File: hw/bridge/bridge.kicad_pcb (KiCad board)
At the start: 2 copper layers, 54.6 x 42.9 mm, 56 parts, among them J1 USB_C_Receptacle_USB2.0_14P, J2 USB_C_Receptacle_USB2.0_14P, J3 DB9, J4 SWD, J5 BOOT, U1 STM32G0B1CBT, U2 MAX485E, U3 CH340E, U4 MCP1754S-3302xCB, U5 TJA1051T-3, U6 74LVC2G240, Y1 HCI XC53G2-8.000-F12NJHP

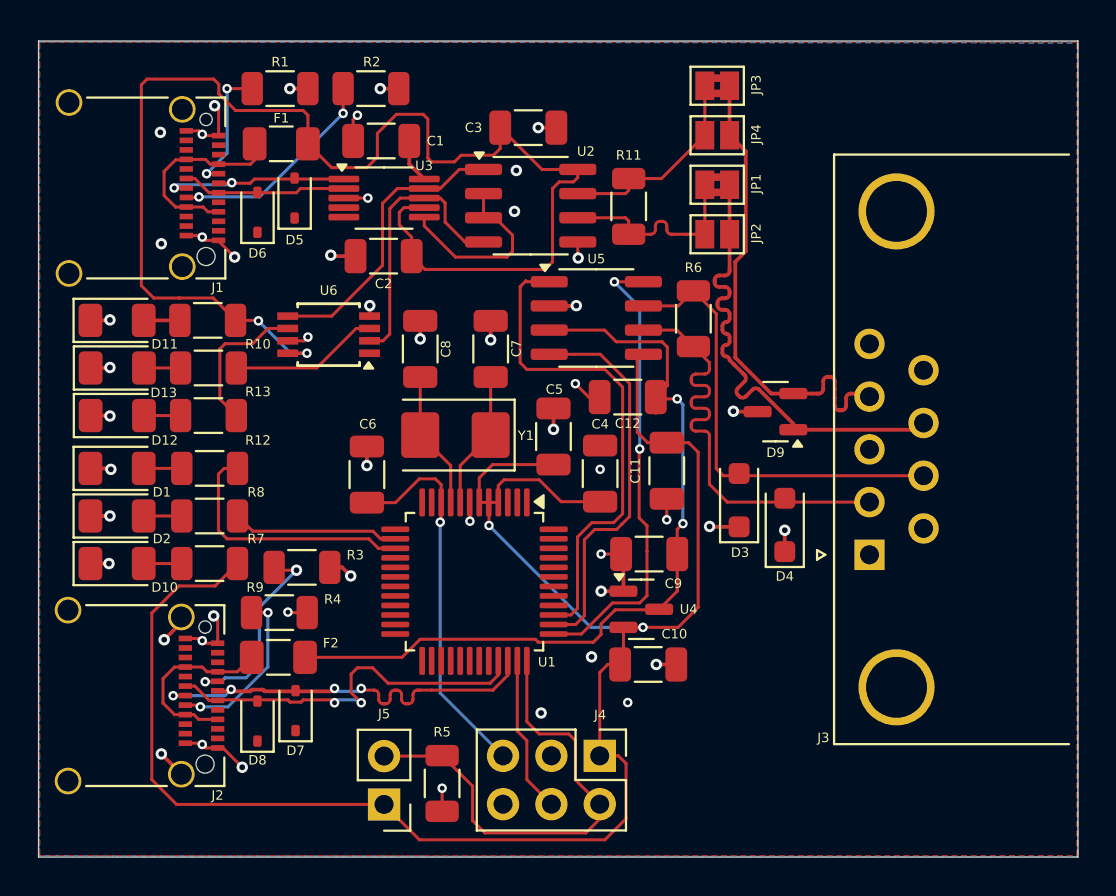
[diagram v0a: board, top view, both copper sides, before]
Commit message: Fix jumpers
Signed-off-by: Mateusz Pająk <22417805+Tai-Min@users.noreply.github.com>
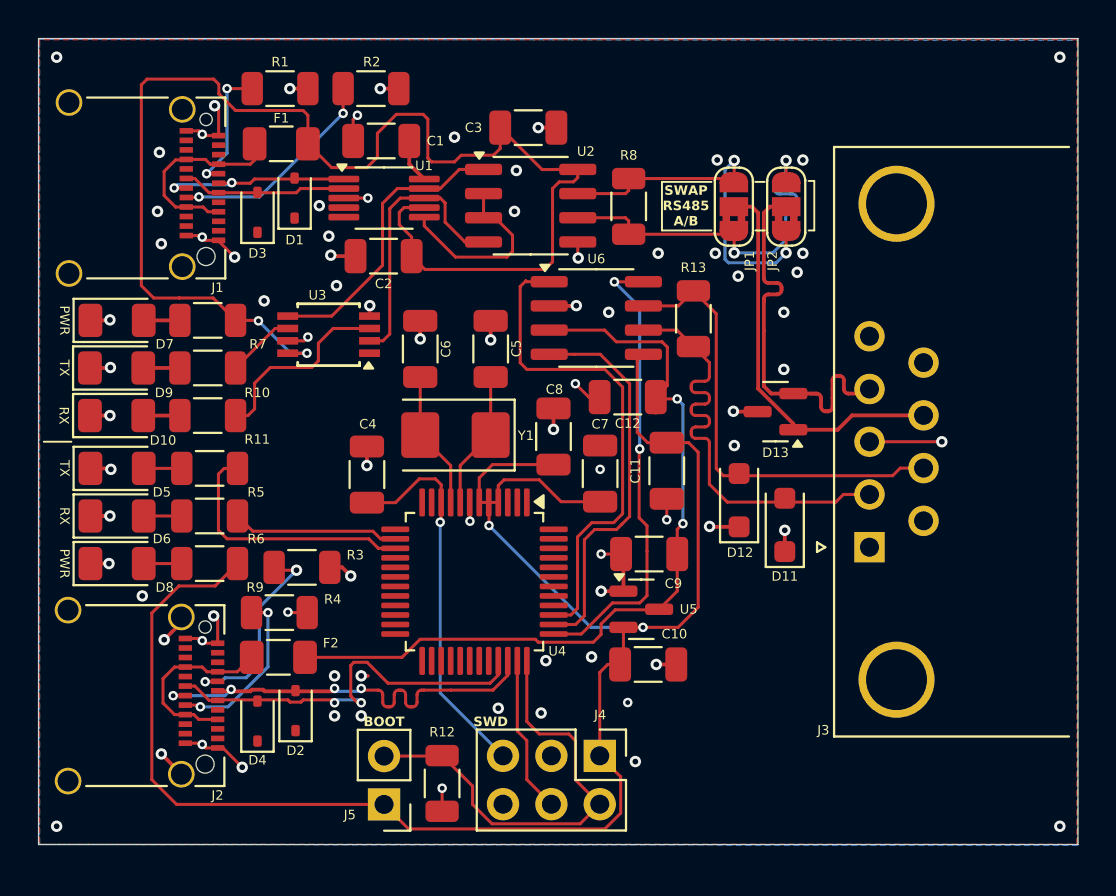
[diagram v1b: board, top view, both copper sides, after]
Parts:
- removed JP3: B, Jumper:SolderJumper-2_P1.3mm_Bridged2Bar_Pad1.0x1.5mm
- removed JP4: A, Jumper:SolderJumper-2_P1.3mm_Open_Pad1.0x1.5mm
- JP1: value A -> JMP; footprint Jumper:SolderJumper-2_P1.3mm_Bridged2Bar_Pad1.0x1.5mm -> Jumper:SolderJumper-3_P1.3mm_Bridged2Bar12_RoundedPad1.0x1.5mm
- JP2: value B -> JMP; footprint Jumper:SolderJumper-2_P1.3mm_Open_Pad1.0x1.5mm -> Jumper:SolderJumper-3_P1.3mm_Bridged2Bar12_RoundedPad1.0x1.5mm
- moved JP2 3.90 mm to (85.8, 112.8), turned to 90 degrees
- moved D10 2.50 mm to (50.6, 123.7)
- moved D9 2.50 mm to (50.6, 121.2)
- moved R10 2.50 mm to (55.4, 121.2)
- moved R11 2.50 mm to (55.4, 123.7)
- moved JP1 1.45 mm to (83.1, 112.8), turned to 90 degrees
- moved J3 0.40 mm to (90.2, 130.6)
- renumbered C6 to C4, C7 to C5, C8 to C6, C4 to C7, C5 to C8, D5 to D1, D13 to D10, D4 to D11, D3 to D12, D9 to D13, D7 to D2, D6 to D3, D8 to D4, D1 to D5, D2 to D6, D11 to D7, D10 to D8, D12 to D9, R12 to R10, R13 to R11, R5 to R12, R6 to R13, R8 to R5, R7 to R6, R10 to R7, R11 to R8, U3 to U1, U6 to U3, U1 to U4, U4 to U5, U5 to U6
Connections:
- JP2 pad 1: /MODBUS+ -> /MODBUS-
- JP2 pad 2: /M+ -> /M-
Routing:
- net /MODBUS-: track 10.9 -> 20.4 mm, vias 0 -> 2
- net /MODBUS+: track 10.9 -> 20.4 mm, vias 0 -> 2
- net /M+: track 25.5 -> 20.7 mm
- net /M-: track 25.6 -> 20.9 mm
- net Net-(R10-Pad2): track 7.87 -> 3.60 mm
- net GND: track 53.9 -> 58.2 mm, vias 50 -> 80
- net Net-(R11-Pad2): track 7.86 -> 10.3 mm
- net +3.3V: track 98.8 -> 97.2 mm
- net /mcu/USB+: track 22.4 -> 23.1 mm
- net /mcu/USB-: track 20.8 -> 21.4 mm
- net /mcu/SWCLK: track 25.2 -> 24.6 mm
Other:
- board size 54.6 x 42.9 mm -> 54.6 x 42.3 mm
- board text added: "BOOT"
- board text added: "PWR"
- board text added: "RX"
- board text added: "SWAP RS485 A/B"
- board text added: "SWD"
- board text added: "TX"

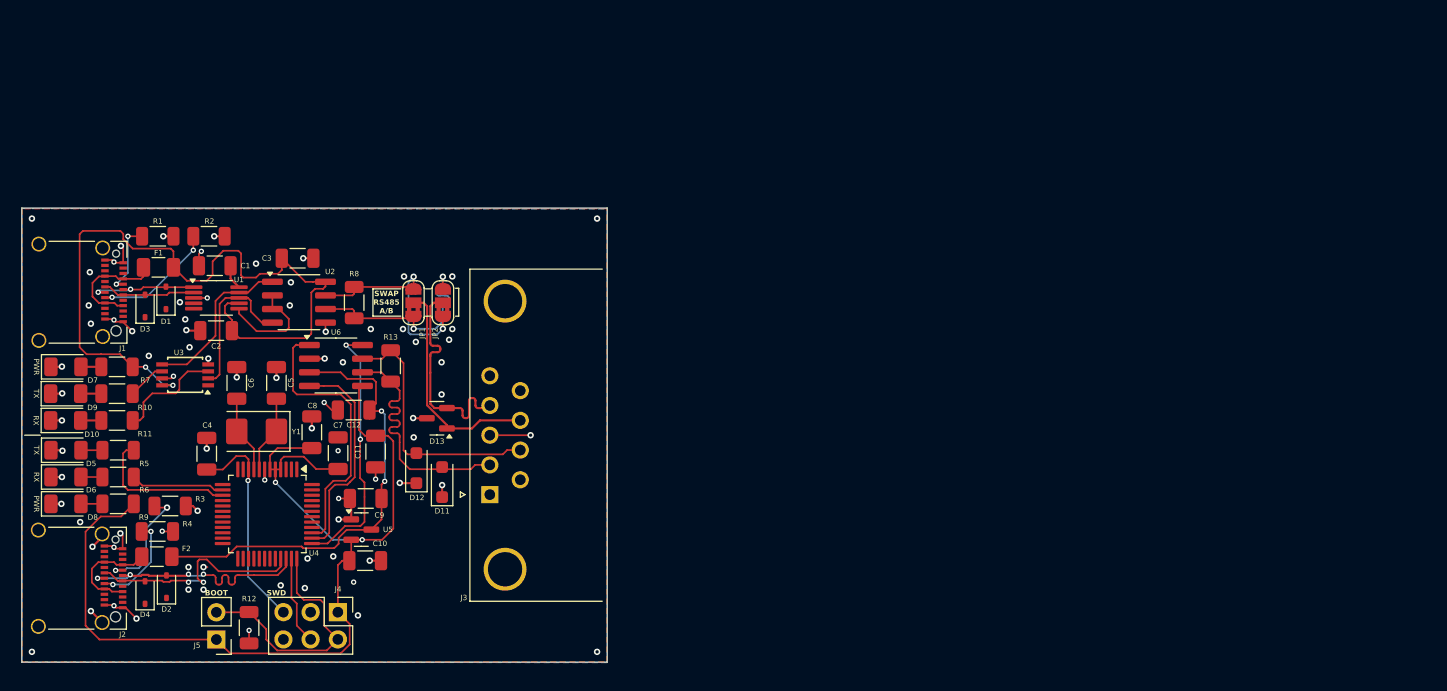
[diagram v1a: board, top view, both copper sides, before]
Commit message: Redesign the PCB, remove DNP components
Signed-off-by: Mateusz Pająk <22417805+Tai-Min@users.noreply.github.com>
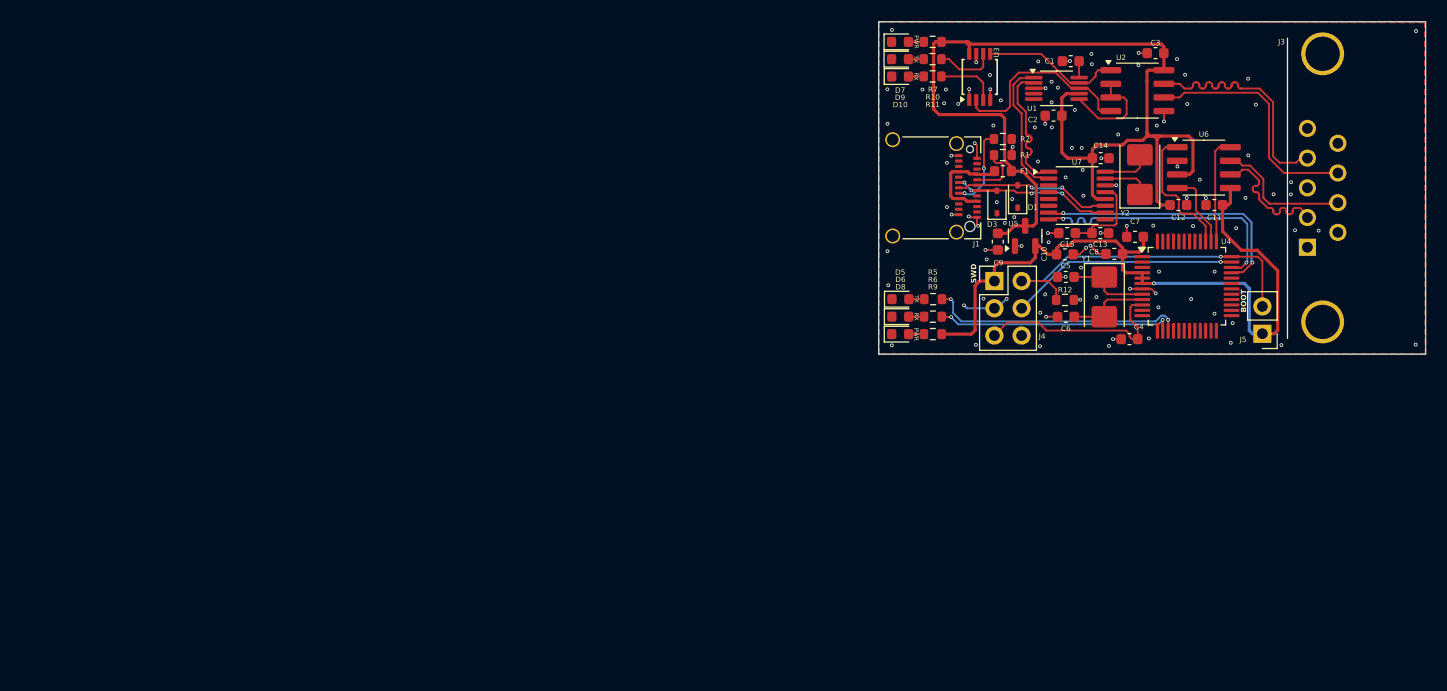
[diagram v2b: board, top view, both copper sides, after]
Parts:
- removed D11, D12: PTVS20VS1UR,115-ES, Diode_SMD:D_SOD-123F
- removed D13: SM712, Package_TO_SOT_SMD:SOT-23
- removed D2, D4: PTVSHC3D4V5B, Diode_SMD:D_SOD-323
- removed F2: 500mA, Fuse:Fuse_1206_3216Metric
- removed J2: USB_C_Receptacle_USB2.0_14P, Connector_USB:USB_C_Receptacle_Amphenol_12401610E4-2A_CircularHoles
- removed JP1, JP2: JMP, Jumper:SolderJumper-3_P1.3mm_Bridged2Bar12_RoundedPad1.0x1.5mm
- removed R13, R8: 120R, Resistor_SMD:R_1206_3216Metric
- removed R3, R4: 5.1k, Resistor_SMD:R_1206_3216Metric
- added C13: 100n / 16V, Capacitor_SMD:C_0603_1608Metric, F.Cu at (147.1, 106.3)
- added C14: 1u / 16V, Capacitor_SMD:C_0603_1608Metric, F.Cu at (147.2, 99.3)
- added C15: 10u / 16V, Capacitor_SMD:C_0603_1608Metric, F.Cu at (144.0, 106.3)
- added U7: CH334R, Package_SO:QSOP-16_3.9x4.9mm_P0.635mm, F.Cu at (144.9, 102.8)
- added Y2: HCI XC53G2-12.000-F20LJDT, Crystal:Crystal_SMD_5032-2Pin_5.0x3.2mm, F.Cu at (150.8, 100.8)
- C1, C10, C11, C12, C2, C3, C5, C7, C8, C9: footprint Capacitor_SMD:C_1206_3216Metric -> Capacitor_SMD:C_0603_1608Metric
- C4: value 100n / 50V -> 100n / 16V; footprint Capacitor_SMD:C_1206_3216Metric -> Capacitor_SMD:C_0603_1608Metric
- C6: value 6p / 50V -> 6p / 16V; footprint Capacitor_SMD:C_1206_3216Metric -> Capacitor_SMD:C_0603_1608Metric
- D10, D5, D6, D7, D8, D9: footprint LED_SMD:LED_1206_3216Metric -> LED_SMD:LED_0603_1608Metric
- F1: footprint Fuse:Fuse_1206_3216Metric -> Fuse:Fuse_0603_1608Metric
- R1, R10, R11, R12, R2, R5, R6, R7, R9: footprint Resistor_SMD:R_1206_3216Metric -> Resistor_SMD:R_0603_1608Metric
- moved J5 101.6 mm to (162.2, 115.6)
- moved U4 88.3 mm to (155.2, 111.2), turned to 0 degrees
- moved C4 86.7 mm to (149.8, 116.1), turned to 0 degrees
- moved D10 84.2 mm to (128.5, 91.7)
- moved D9 83.8 mm to (128.4, 90.0)
- moved D7 83.5 mm to (128.4, 88.4)
- moved U6 83.0 mm to (156.8, 100.2)
- moved R11 82.5 mm to (131.5, 91.6)
- moved C3 82.2 mm to (152.3, 89.5), turned to 0 degrees
- moved R10 82.2 mm to (131.5, 90.0)
- moved C1 82.1 mm to (144.4, 90.2)
- moved R12 82.0 mm to (143.8, 112.5), turned to 0 degrees
- moved R7 81.9 mm to (131.5, 88.4)
- moved C11 81.5 mm to (157.8, 103.6), turned to 0 degrees
- moved U1 80.7 mm to (143.0, 92.8)
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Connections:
- net /can/RX renamed /mcu/CAN_RX
- net /can/S renamed /mcu/CAN_S
- net /can/TX renamed /mcu/CAN_TX
- C12 pad 2: +5C -> +5V
- C9 pad 2: +5C -> +5V
- D1 pad 2: /RS_D+ -> /D+
- D3 pad 2: /RS_D- -> /D-
- J1 pad A6: /RS_D+ -> /D+
- J1 pad A7: /RS_D- -> /D-
- J1 pad B6: /RS_D+ -> /D+
- J1 pad B7: /RS_D- -> /D-
- U1 pad 1: /RS_D+ -> /D_RS+
- U1 pad 2: /RS_D- -> /D_RS-
- U2 pad 6: /MODBUS+ -> /M+
- U2 pad 7: /MODBUS- -> /M-
- U4 pad 33: /mcu/USB- -> /D_CAN-
- U4 pad 34: /mcu/USB+ -> /D_CAN+
- U5 pad 3: +5C -> +5V
- U6 pad 3: +5C -> +5V
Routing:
- net +5C: track 43.3 -> 0.00 mm, vias 2 -> 0
- net +3.3V: track 97.2 -> 67.6 mm, vias 2 -> 1
- net +5V: track 72.0 -> 101.3 mm, vias 2 -> 0
- net /D_CAN-: track 0.00 -> 25.5 mm, vias 0 -> 2
- net /D_CAN+: track 0.00 -> 25.4 mm, vias 0 -> 2
- net GND: track 58.2 -> 34.6 mm, vias 80 -> 109
- net /mcu/USB+: track 23.1 -> 0.00 mm, vias 4 -> 0
- net /mcu/USB-: track 21.4 -> 0.00 mm, vias 2 -> 0
- net /MODBUS-: track 20.4 -> 0.00 mm, vias 2 -> 0
- net /MODBUS+: track 20.4 -> 0.00 mm, vias 2 -> 0
- net /D-: track 0.00 -> 16.9 mm, vias 0 -> 4
- net /D+: track 0.00 -> 14.8 mm, vias 0 -> 2
- net /mcu/CAN_S: track 24.5 -> 10.0 mm, vias 2 -> 0
- net /mcu/LED_RX: track 8.78 -> 22.2 mm, vias 0 -> 2
- net /mcu/CAN_TX: track 26.3 -> 12.9 mm
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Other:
- board size 54.6 x 42.3 mm -> 51 x 31 mm
- board text removed: "SWAP RS485 A/B"

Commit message: Add datasheets, add BOM links
Signed-off-by: Mateusz Pająk <22417805+Tai-Min@users.noreply.github.com>
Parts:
- C1: value 100n -> 100n / 16V
- C6: value 6p / 16V -> 6p / 50V
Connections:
- net /M+ renamed /MODBUS+
- net /M- renamed /MODBUS-

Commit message: Minor fixes
Signed-off-by: Mateusz Pająk <22417805+Tai-Min@users.noreply.github.com>
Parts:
- removed the U3 at (135.9, 91.7)
- added C4: 1u, Capacitor_SMD:C_0603_1608Metric, F.Cu at (133.1, 108.6)
- added R12: 0, Resistor_SMD:R_0603_1608Metric, F.Cu at (162.1, 99.4)
- added R13: 0, Resistor_SMD:R_0603_1608Metric, F.Cu at (162.1, 100.9)
- added R14: 0, Resistor_SMD:R_0603_1608Metric, F.Cu at (155.9, 93.7)
- added R15: 0, Resistor_SMD:R_0603_1608Metric, F.Cu at (155.9, 92.2)
- added R3: 10k, Resistor_SMD:R_0603_1608Metric, F.Cu at (138.5, 89.4)
- added R4: 10k, Resistor_SMD:R_0603_1608Metric, F.Cu at (151.4, 104.7)
- added REF**: OSHW-Logo2_7.3x6mm_SilkScreen, Symbol:OSHW-Logo2_7.3x6mm_SilkScreen, F.Cu at (160.6, 92.5)
- added REF**: KiCad-Logo2_5mm_SilkScreen, Symbol:KiCad-Logo2_5mm_SilkScreen, B.Cu at (134.0, 90.2)
- added U4: 74LVC2G04, Package_TO_SOT_SMD:SOT-23-6, F.Cu at (135.4, 91.2)
- C1: renamed from C2; value 100n / 16V -> 100n
- C10: renamed from C11; value 100n / 16V -> 100n
- C11: renamed from C12; value 100n / 16V -> 100n
- C12: renamed from C4; value 100n / 16V -> 100n
- C13: renamed from C5; value 6p / 50V -> 6p
- C14: renamed from C6; value 6p / 50V -> 6p
- C15: renamed from C7; value 100n / 16V -> 100n
- C16: renamed from C8; value 100n / 16V -> 100n
- C2: renamed from C1; value 100n / 16V -> 100n
- C3: value 100n / 16V -> 100n
- C5: renamed from C15; value 10u / 16V -> 10u
- C6: renamed from C13; value 100n / 16V -> 100n
- C7: renamed from C14; value 1u / 16V -> 1u
- C8: renamed from C9; value 10u / 16V -> 10u
- C9: renamed from C10; value 10u / 16V -> 10u
- J2: renamed from J3; value DB9 -> DE9
- moved C3 27.9 mm to (133.5, 110.1), turned to 180 degrees
- moved D5 3.14 mm to (128.5, 91.6)
- moved R7 3.14 mm to (131.5, 91.6)
- moved D3 1.69 mm to (128.4, 88.3)
- moved D4 1.69 mm to (128.5, 90.0)
- moved R5 1.69 mm to (131.5, 88.3)
- moved R6 1.69 mm to (131.5, 90.0)
- renumbered D3 to D2, D9 to D3, D10 to D4, D7 to D5, D5 to D6, D6 to D7, J4 to J3, J5 to J4, R9 to R10, R12 to R11, R10 to R5, R11 to R6, R5 to R8, R6 to R9, U7 to U3, U4 to U7, Y2 to Y1, Y1 to Y2
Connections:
- C3 pad 2: +5V -> /VUSB
- F1 pad 1: Net-(F1-Pad1) -> /VUSB
- J1 pad A4: Net-(F1-Pad1) -> /VUSB
- J1 pad A9: Net-(F1-Pad1) -> /VUSB
- J1 pad B4: Net-(F1-Pad1) -> /VUSB
- J1 pad B9: Net-(F1-Pad1) -> /VUSB
- U2 pad 6: /MODBUS+ -> Net-(U2-A)
- U2 pad 7: /MODBUS- -> Net-(U2-B)
- U3 pad 9: unconnected-(U7-~{RESET}/CDP-Pad9) -> Net-(U3-~{RESET}/CDP)
- U6 pad 6: /CAN- -> Net-(U6-CANL)
- U6 pad 7: /CAN+ -> Net-(U6-CANH)
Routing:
- net /VUSB: track 0.00 -> 17.6 mm
- net Net-(U3-~{RESET}/CDP): track 0.00 -> 10.3 mm, vias 0 -> 2
- net Net-(F1-Pad1): track 9.15 -> 0.00 mm
- net /MODBUS-: track 22.4 -> 18.6 mm
- net +5V: track 101.3 -> 97.5 mm
- net /MODBUS+: track 22.5 -> 18.8 mm
- net Net-(R6-Pad2): track 5.75 -> 2.09 mm
- net /CAN+: track 12.8 -> 9.20 mm
- net /CAN-: track 12.6 -> 9.16 mm
- net +3.3V: track 67.6 -> 70.4 mm
- net GND: track 34.6 -> 36.9 mm, vias 109 -> 177
- net Net-(U6-CANL): track 0.00 -> 2.05 mm
- net Net-(U2-B): track 0.00 -> 2.04 mm
- net Net-(U6-CANH): track 0.00 -> 2.04 mm
- net Net-(U2-A): track 0.00 -> 2.03 mm
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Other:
- board text added: "${TITLE} REV:${REVISION}"
- board text added: "github.com/Tai-Min/Robo-Bus"

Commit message: Add hub crystal-free alternative, add hub rst pull up, replace usbc with tht alternative
Signed-off-by: Mateusz Pająk <22417805+Tai-Min@users.noreply.github.com>
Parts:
- removed the C4 at (133.1, 108.6)
- added R7: 0, Resistor_SMD:R_0603_1608Metric, F.Cu at (142.4, 98.4)
- C3: value 100n -> 10n
- J1: footprint Connector_USB:USB_C_Receptacle_Amphenol_12401610E4-2A_CircularHoles -> Connector_USB:USB_C_Receptacle_GCT_USB4085
- moved J1 4.89 mm to (134.5, 99.1)
- moved C3 1.47 mm to (133.5, 108.7)
- renumbered C11 to C10, C12 to C11, C13 to C12, C14 to C13, C15 to C14, C16 to C15, C5 to C4, C6 to C5, C7 to C6, C8 to C7, C9 to C8, C10 to C9, R7 to R10, R8 to R11, R9 to R12, R10 to R13, R12 to R14, R13 to R15, R11 to R16, R14 to R4, R15 to R5, R4 to R6, R5 to R8, R6 to R9
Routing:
- net Net-(U3-XI): track 4.57 -> 10.9 mm, vias 0 -> 2
- net GND: track 36.9 -> 41.0 mm, vias 177 -> 171
- net Net-(J1-CC2): track 7.79 -> 10.3 mm, vias 2 -> 1
- net Net-(J1-CC1): track 5.17 -> 6.51 mm
- net /D+: track 14.8 -> 15.8 mm
- net /VUSB: track 17.6 -> 18.6 mm
- net /D-: track 16.9 -> 17.6 mm, vias 4 -> 2

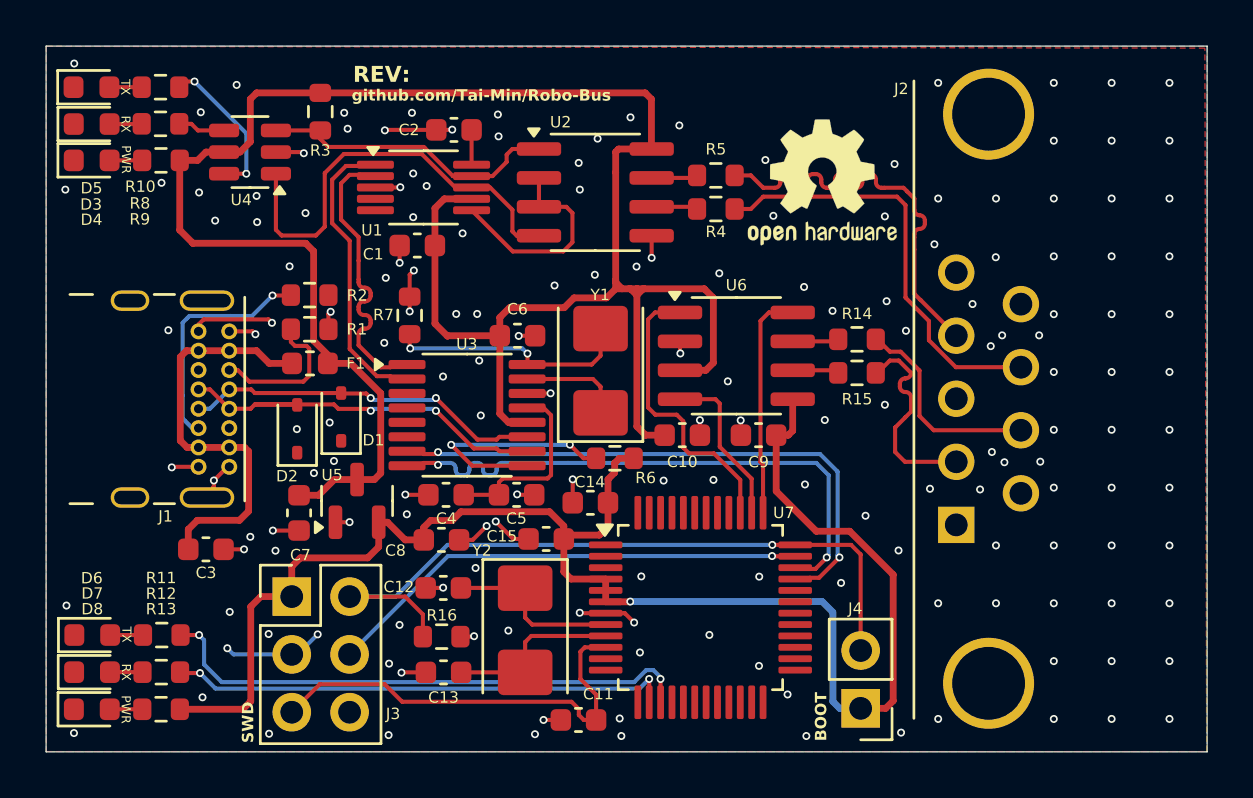
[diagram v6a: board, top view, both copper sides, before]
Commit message: Manufacture fixes
Signed-off-by: Mateusz Pająk <22417805+Tai-Min@users.noreply.github.com>
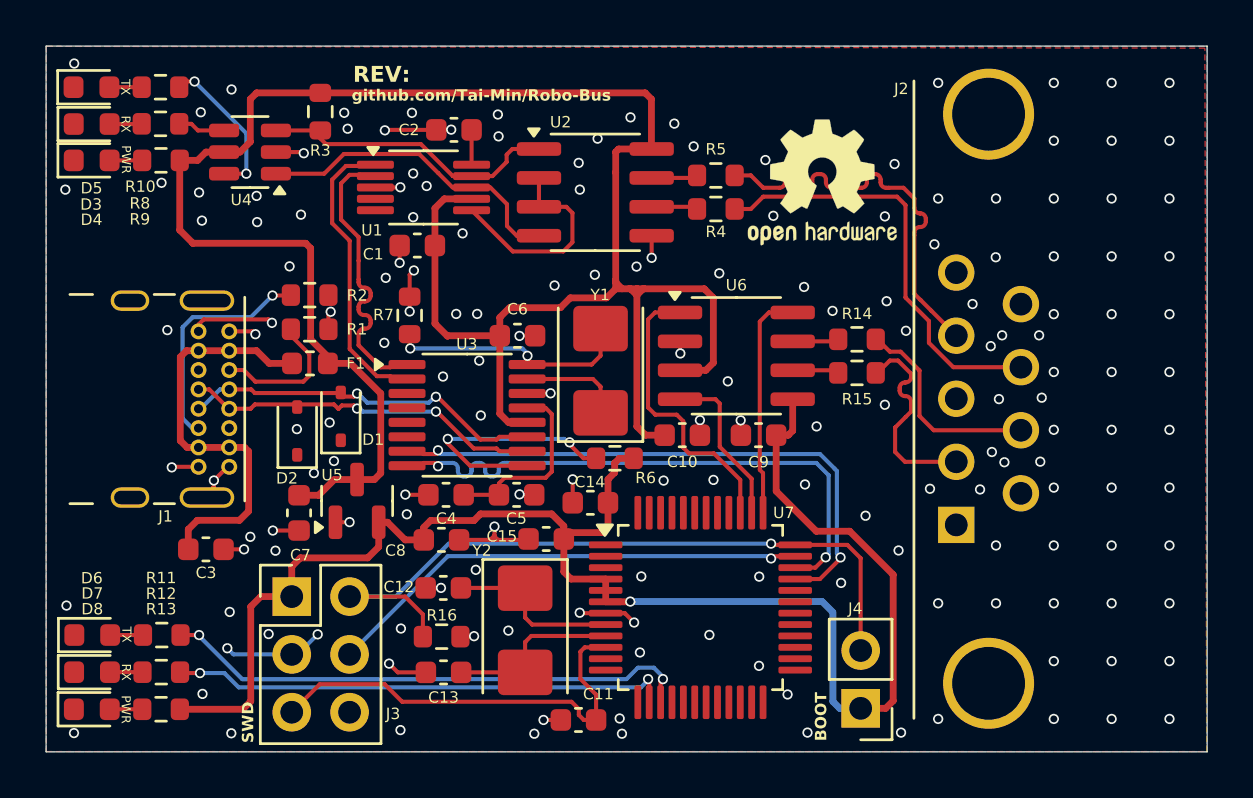
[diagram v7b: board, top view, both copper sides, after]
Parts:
- R1, R2: value 5.1k -> 5.1K
- R10, R11, R12, R13, R8, R9: value 1k -> 1K
- R14, R15, R4, R5, R7: value 0 -> 0R
- R16, R3, R6: value 10k -> 10K
- moved D2 0.09 mm to (137.5, 103.5)
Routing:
- net /TX: track 19.0 -> 14.0 mm
- net /D-: track 17.6 -> 15.9 mm
- net GND: track 41.0 -> 42.6 mm, vias 171 -> 172
- net Net-(U3-~{RESET}/CDP): track 10.3 -> 11.0 mm
